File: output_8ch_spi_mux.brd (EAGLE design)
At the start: 65 x 56 mm, 50 parts, among them IC1 TPS706-1V8, IC2 5M160ZE64, IC3 SN75174SOIC-20, IC4 SN75174SOIC-20, IC6 STM32F042F, IC7 CAT24C256, Q1 50MHz

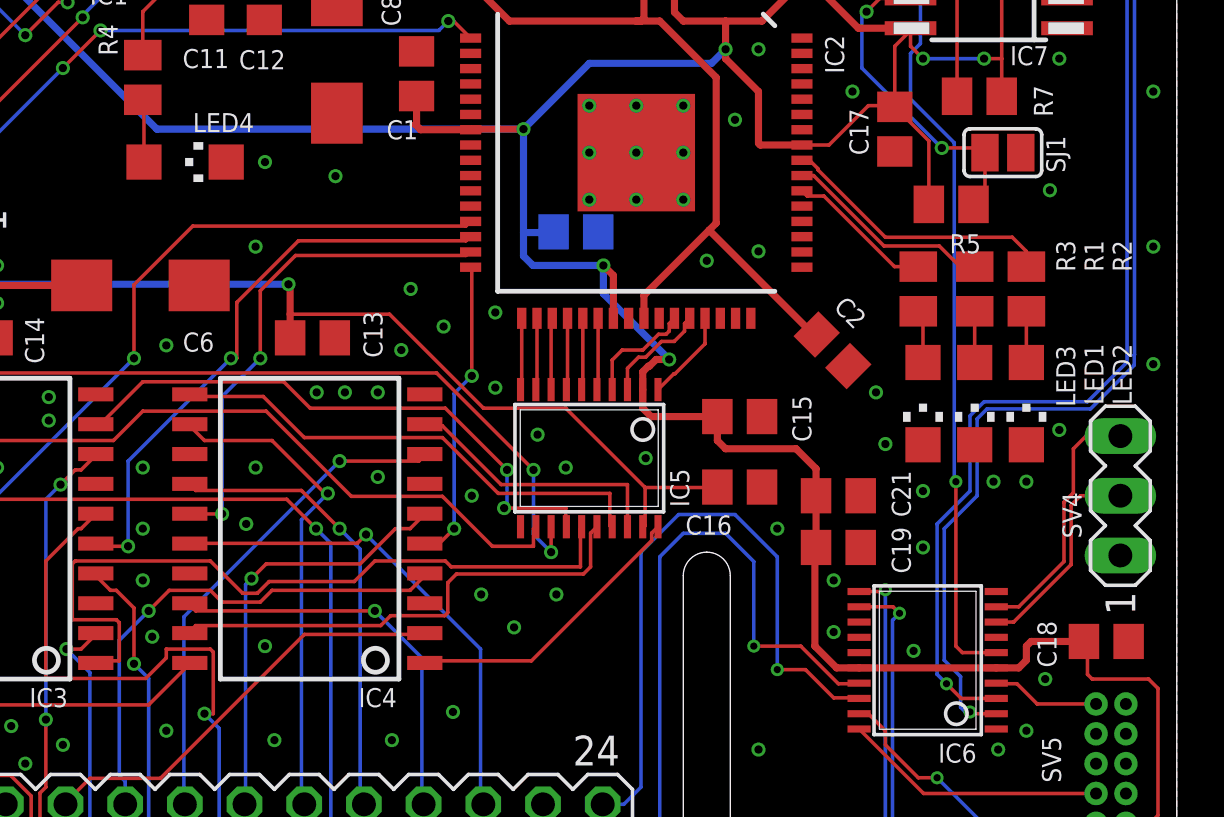
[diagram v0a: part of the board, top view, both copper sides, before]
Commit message: Added I2C testpoints
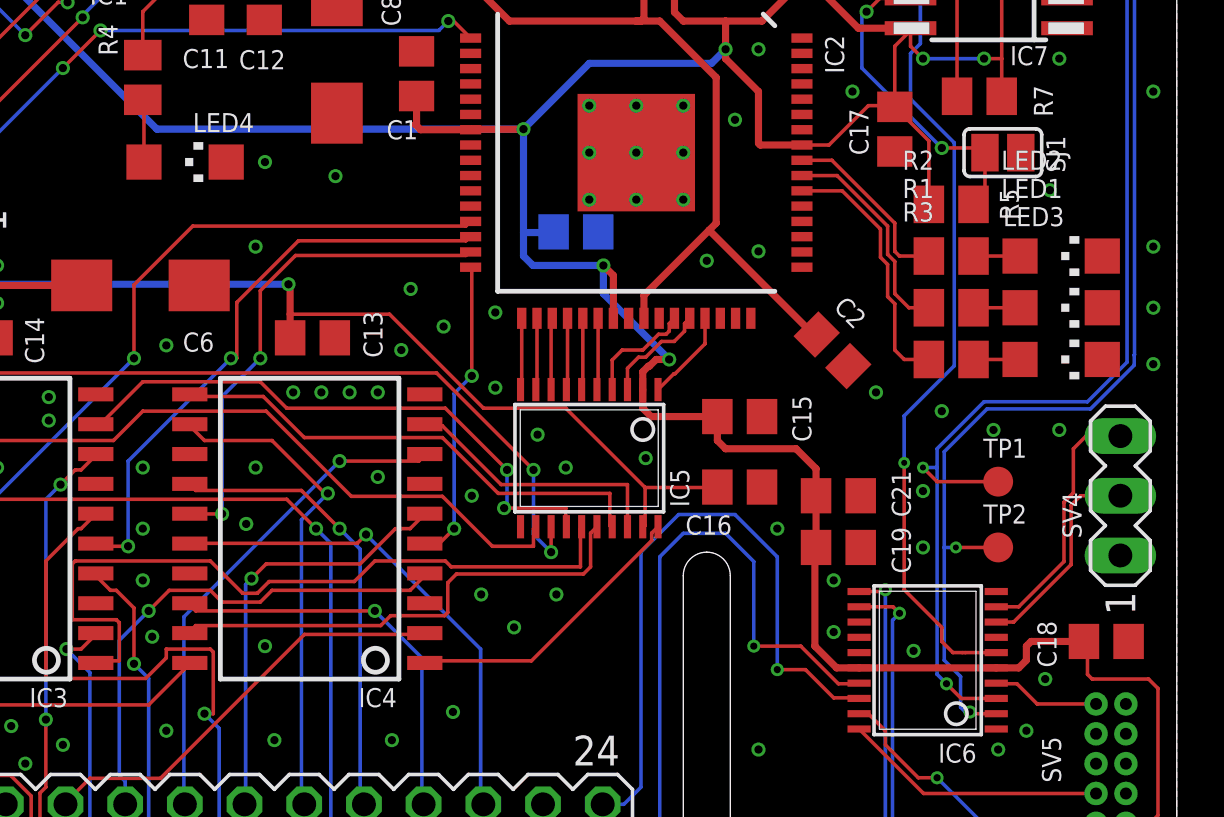
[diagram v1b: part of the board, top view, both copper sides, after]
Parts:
- added TP1, TP2: PTR1B1,27, testpad:B1,27
- moved LED2 6.45 mm to (60.1, 32.6), turned to 270 degrees
- moved LED3 6.17 mm to (60.1, 28.2), turned to 270 degrees
- moved LED1 5.49 mm to (60.1, 30.4), turned to 270 degrees
- moved R2 3.49 mm to (55.4, 32.6), turned to 0 degrees
- moved R3 3.31 mm to (55.4, 28.2), turned to 0 degrees
- moved R1 1.28 mm to (55.4, 30.4), turned to 0 degrees
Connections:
- net I2C_SCL: now also TP1.TP
- net I2C_SDA: now also TP2.TP
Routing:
- net STATUS2: track 6.29 -> 11.0 mm
- net I2C_SCL: track 99.8 -> 103.8 mm, vias 1 -> 2
- net STATUS1: track 11.8 -> 7.79 mm
- net I2C_SDA: track 103.6 -> 105.9 mm, vias 1 -> 2
- net !CAN_INT: track 38.1 -> 40.1 mm

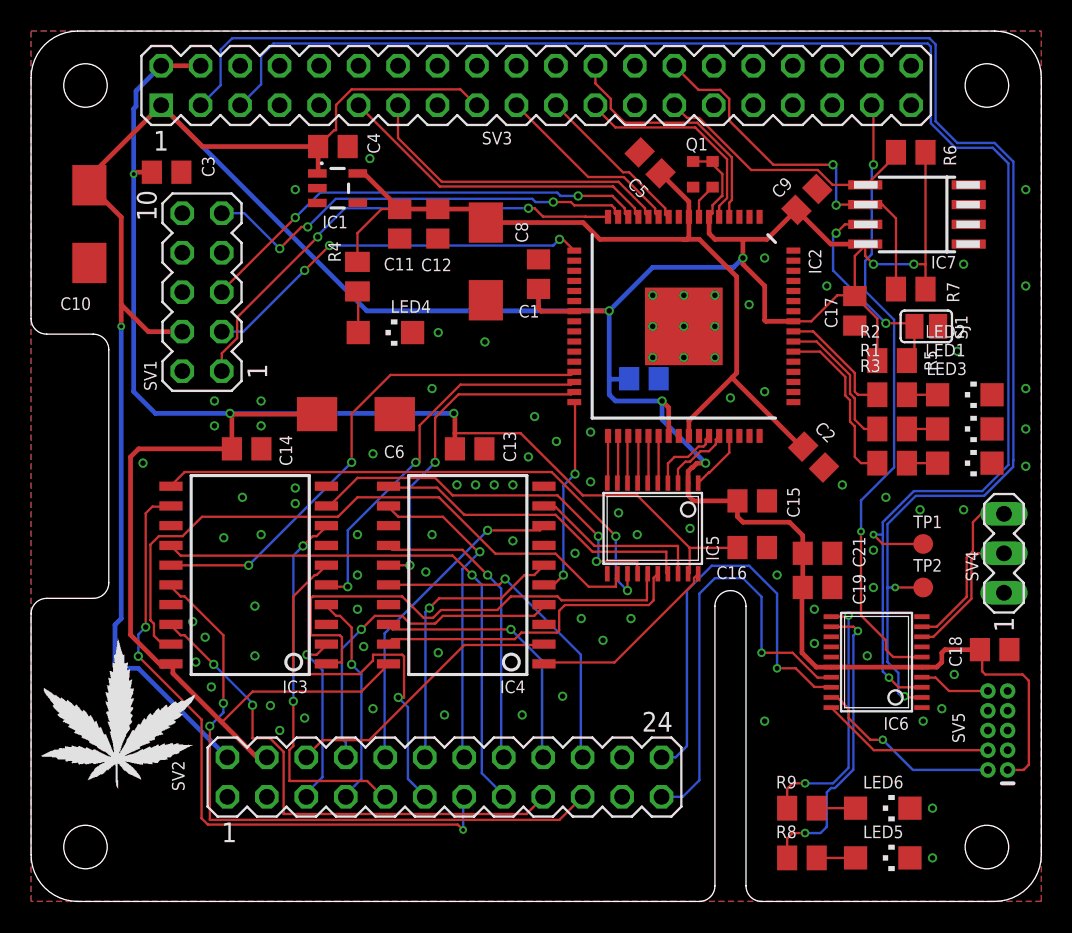
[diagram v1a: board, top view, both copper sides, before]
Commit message: Added clock calibration signal to cannabus controller (divide 50MHz clk by 1000 in CPLD)
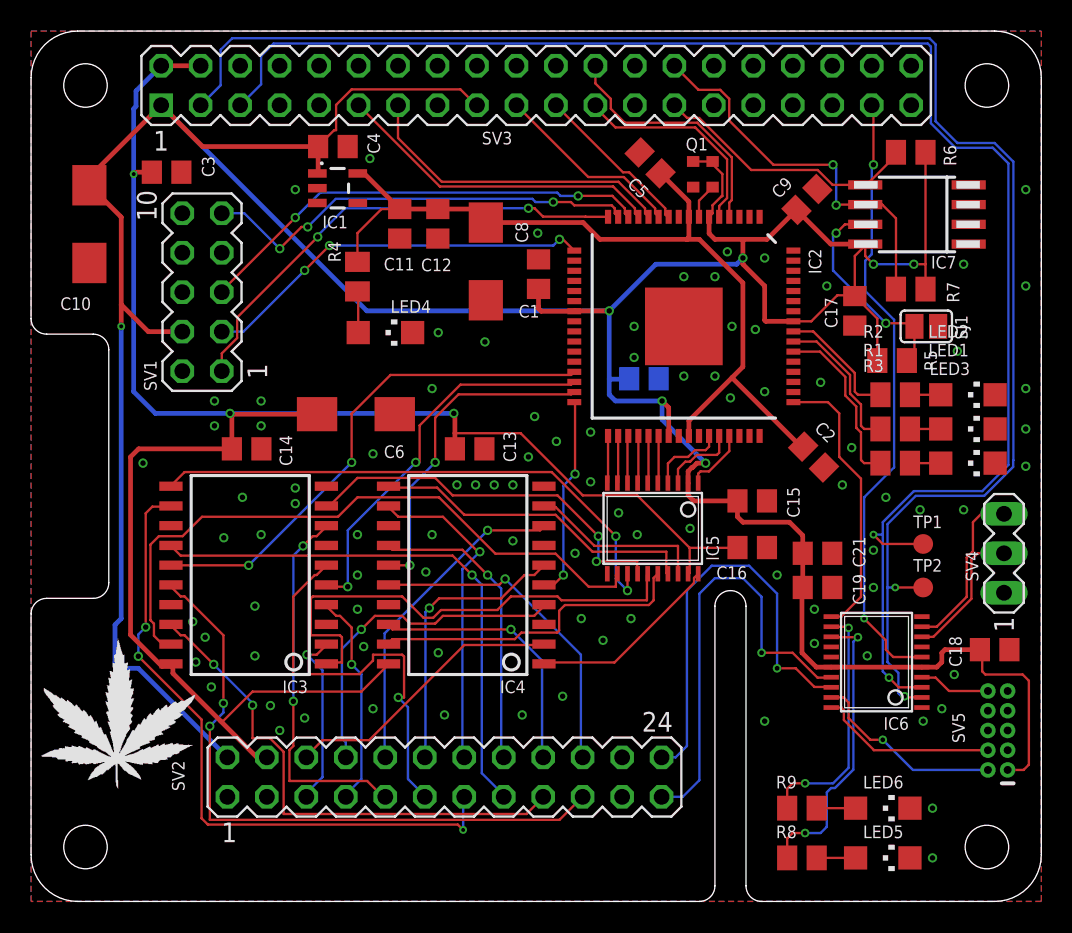
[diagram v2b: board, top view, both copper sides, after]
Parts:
- moved LED1 0.20 mm to (60.3, 30.4)
- moved LED2 0.20 mm to (60.3, 32.6)
- moved LED3 0.20 mm to (60.3, 28.2)
- moved R1 0.20 mm to (55.6, 30.4)
- moved R2 0.20 mm to (55.6, 32.6)
- moved R3 0.20 mm to (55.6, 28.2)
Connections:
- new net OSC_CAL_CLK: IC2.49, IC6.11
- net CORTEX_STATUS0: now also IC6.13; no longer IC6.12
- net CORTEX_STATUS1: now also IC6.12; no longer IC6.11
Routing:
- net OSC_CAL_CLK: track 0.00 -> 18.1 mm
- net CORTEX_STATUS1: track 16.7 -> 15.9 mm
- net CORTEX_SWDIO: track 12.4 -> 13.0 mm
- net CORTEX_STATUS0: track 19.5 -> 19.0 mm

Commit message: Cleaned up output and differential driver boards; added basic differential receiver board
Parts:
- moved C4 2.33 mm to (18.2, 46.6)
- moved IC1 2.33 mm to (18.5, 43.9)
- moved C1 1.00 mm to (31.6, 40.4)
- moved C8 0.82 mm to (28.5, 41.4)
- moved C12 0.82 mm to (25.4, 43.8)
- moved C11 0.45 mm to (23.3, 43.8)
- moved C3 0.40 mm to (8.72, 47.3)
- moved R5 0.20 mm to (55.6, 34.8)
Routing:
- net +3V3: track 243.8 -> 249.4 mm, vias 7 -> 8
- net CPLD_TDI: track 28.4 -> 30.6 mm
- net CPLD_TDO: track 25.4 -> 27.2 mm
- net VCORE: track 55.7 -> 54.6 mm
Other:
- board text added: "Rev 01"

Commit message: yes
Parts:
- LED5, LED6: value (none) -> GRN
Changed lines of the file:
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@@
 </class>
 </classes>
-<designrules name="oshpark-2layer">
+<designrules name="oshpark-2layer *">
 <description language="en">&lt;b&gt;OSH Park Design Rules&lt;/b&gt;
 &lt;p&gt;
@@
 <param name="checkValues" value="0"/>
 <param name="checkNames" value="1"/>
-<param name="checkWireStubs" value="1"/>
+<param name="checkWireStubs" value="0"/>
 <param name="checkPolygonWidth" value="0"/>
 <param name="useDiameter" value="13"/>
@@
 <attribute name="SPICEPREFIX" value="C" x="28.46" y="41.38" size="1.778" layer="27" rot="R270" display="off"/>
 </element>
-<element name="IC1" library="lichtenstein_onion" package="SOT23-5" value="TPS706-1V8" x="18.52" y="43.89" smashed="yes" rot="R270">
+<element name="IC1" library="lichtenstein_onion" package="SOT23-5" package3d_urn="urn:adsk.eagle:package:16456/2" value="TPS706-1V8" x="18.52" y="43.89" smashed="yes" rot="R270">
 <attribute name="MOUSER" value="595-TPS70618DBVT" x="18.52" y="43.89" size="1.778" layer="27" rot="R270" display="off"/>
 <attribute name="NAME" x="19.179" y="42.121" size="0.8128" layer="25" font="vector" ratio="10" rot="R180"/>
@@
 <attribute name="NAME" x="50.035" y="42" size="0.8128" layer="25" font="vector" ratio="10" rot="R270"/>
 </element>
-<element name="IC5" library="lichtenstein_onion" package="TSSOP20" value="" x="40" y="24" smashed="yes" rot="R180">
+<element name="IC5" library="lichtenstein_onion" package="TSSOP20" package3d_urn="urn:adsk.eagle:package:4349/2" value="" x="40" y="24" smashed="yes" rot="R180">
 <attribute name="MOUSER" value="595-TXB0108PWR" x="40" y="24" size="1.778" layer="27" rot="R180" display="off"/>
 <attribute name="NAME" x="44.2544" y="21.9172" size="0.8128" layer="25" font="vector" ratio="10" rot="R90"/>
@@
 <attribute name="SPICEPREFIX" value="C" x="50.6" y="20.2" size="1.778" layer="27" display="off"/>
 </element>
-<element name="IC6" library="lichtenstein_onion" package="TSSOP20" value="STM32F042F" x="54.4" y="15.4" smashed="yes" rot="R90">
+<element name="IC6" library="lichtenstein_onion" package="TSSOP20" package3d_urn="urn:adsk.eagle:package:4349/2" value="STM32F042F" x="54.4" y="15.4" smashed="yes" rot="R90">
 <attribute name="MOUSER" value="511-STM32F042F6P6" x="54.4" y="15.4" size="1.016" layer="27" rot="R90" display="off"/>
 <attribute name="NAME" x="56.4828" y="11.8544" size="0.8128" layer="25" ratio="10" rot="R180"/>
 </element>
-<element name="LED5" library="led" library_urn="urn:adsk.eagle:library:259" package="CHIPLED_1206" package3d_urn="urn:adsk.eagle:package:15823/2" value="" x="54.8" y="2.8" smashed="yes" rot="R270">
+<element name="LED5" library="led" library_urn="urn:adsk.eagle:library:259" package="CHIPLED_1206" package3d_urn="urn:adsk.eagle:package:15823/2" value="GRN" x="54.8" y="2.8" smashed="yes" rot="R270">
 <attribute name="MOUSER" value="604-APTR3216SGC" x="66.8" y="9.2" size="1.016" layer="27" rot="R270" display="off"/>
 <attribute name="NAME" x="53.53" y="4.07" size="0.8128" layer="25" ratio="10"/>
-<attribute name="VALUE" x="53.53" y="0.26" size="1.27" layer="27"/>
 </element>
 <element name="R8" library="rcl" library_urn="urn:adsk.eagle:library:334" package="M0805" package3d_urn="urn:adsk.eagle:package:23556/1" value="680R" x="49.6" y="2.8" smashed="yes">
@@
 <attribute name="SPICEPREFIX" value="R" x="49.6" y="6" size="1.016" layer="27" display="off"/>
 </element>
-<element name="LED6" library="led" library_urn="urn:adsk.eagle:library:259" package="CHIPLED_1206" package3d_urn="urn:adsk.eagle:package:15823/2" value="" x="54.8" y="6" smashed="yes" rot="R270">
+<element name="LED6" library="led" library_urn="urn:adsk.eagle:library:259" package="CHIPLED_1206" package3d_urn="urn:adsk.eagle:package:15823/2" value="GRN" x="54.8" y="6" smashed="yes" rot="R270">
 <attribute name="MOUSER" value="604-APTR3216SGC" x="54.8" y="6" size="1.016" layer="27" rot="R270" display="off"/>
 <attribute name="NAME" x="53.53" y="7.27" size="0.8128" layer="25" ratio="10"/>
-<attribute name="VALUE" x="53.53" y="3.46" size="1.27" layer="27"/>
 </element>
 <element name="SV4" library="con-lstb" library_urn="urn:adsk.eagle:library:162" package="MA03-1" package3d_urn="urn:adsk.eagle:package:8339/1" value="" x="62.6" y="22.4" smashed="yes" rot="R90">
@@
 <wire x1="40.50175" y1="46.848246875" x2="42.325" y2="45.024996875" width="0.3048" layer="1"/>
 <wire x1="42.325" y1="45.024996875" x2="42.325" y2="44.05" width="0.3048" layer="1"/>
-<wire x1="19.8201" y1="44.84" x2="21" y2="44.84" width="0.3048" layer="1"/>
+<wire x1="19.826" y1="44.84" x2="21" y2="44.84" width="0.3048" layer="1"/>
 <wire x1="21" y1="44.84" x2="23.31" y2="44.84" width="0.3048" layer="1"/>
 <wire x1="23.31" y1="44.84" x2="23.4" y2="44.75" width="0.3048" layer="1"/>
@@
 <via x="15.4" y="44.8" extent="1-16" drill="0.35"/>
 <wire x1="15.4" y1="44.8" x2="17.1799" y2="44.8" width="0.3048" layer="1"/>
-<wire x1="17.1799" y1="44.8" x2="17.2199" y2="44.84" width="0.3048" layer="1"/>
+<wire x1="17.1799" y1="44.8" x2="17.214" y2="44.84" width="0.3048" layer="1"/>
 <wire x1="17.27" y1="46.57" x2="17.2199" y2="46.5199" width="0.3048" layer="1"/>
-<wire x1="17.2199" y1="46.5199" x2="17.2199" y2="44.84" width="0.3048" layer="1"/>
+<wire x1="17.2199" y1="46.5199" x2="17.214" y2="44.84" width="0.3048" layer="1"/>
 <wire x1="28.69" y1="49.89" x2="28.4" y2="49.6" width="0.3048" layer="16"/>
 <wire x1="28.69" y1="49.89" x2="28.69" y2="51.23" width="0.3048" layer="16"/>
@@
 <wire x1="52" y1="28.6" x2="53.4" y2="27.2" width="0.1524" layer="1"/>
 <wire x1="53.4" y1="27.2" x2="53.4" y2="19.6" width="0.1524" layer="1"/>
-<wire x1="52.125" y1="18.325" x2="51.4822" y2="18.325" width="0.1524" layer="1"/>
 <wire x1="51.275" y1="32.125" x2="52" y2="31.4" width="0.1524" layer="1"/>
 <wire x1="52" y1="31.4" x2="52" y2="28.6" width="0.1524" layer="1"/>
 <wire x1="53.4" y1="19.6" x2="52.125" y2="18.325" width="0.1524" layer="1"/>
+<wire x1="52.125" y1="18.325" x2="51.4822" y2="18.325" width="0.1524" layer="1"/>
 </signal>
 </signals>

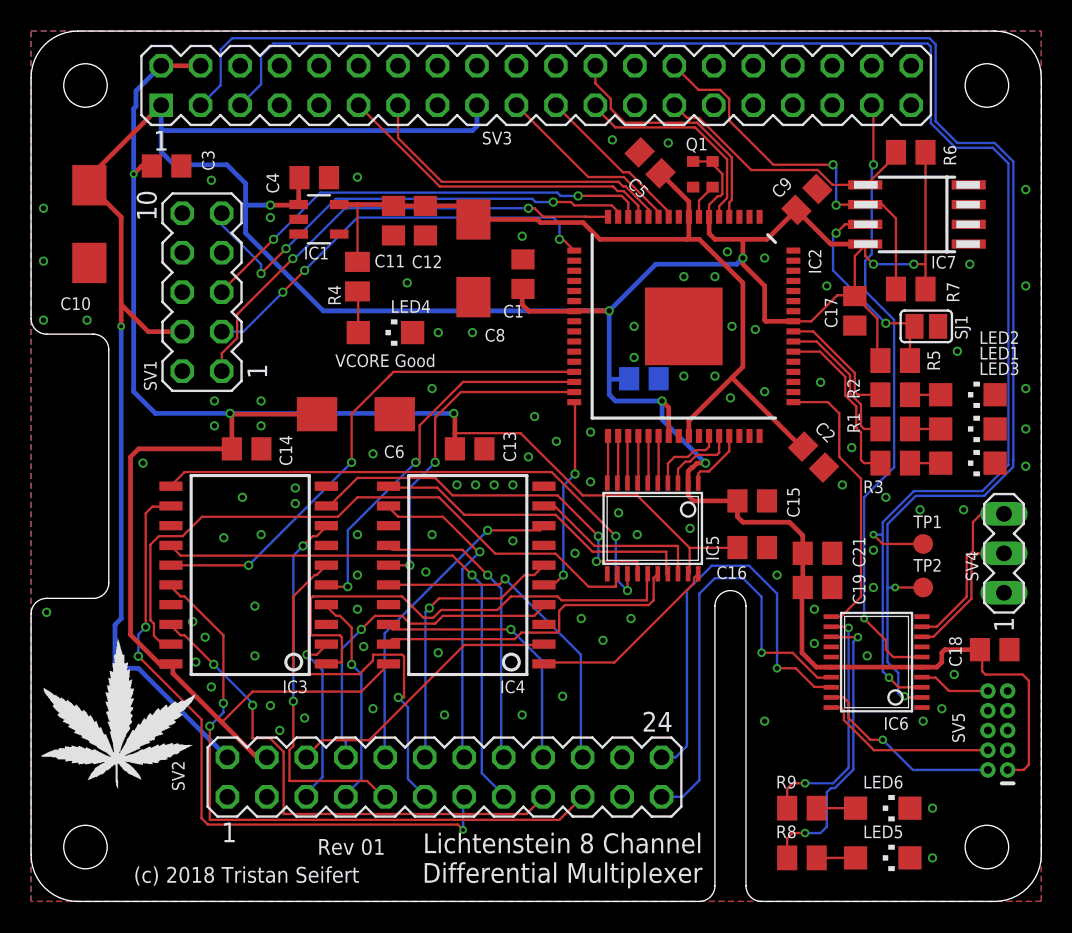
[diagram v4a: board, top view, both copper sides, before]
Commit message: rev01 of output_8ch_spi_mux sent to manufacturing
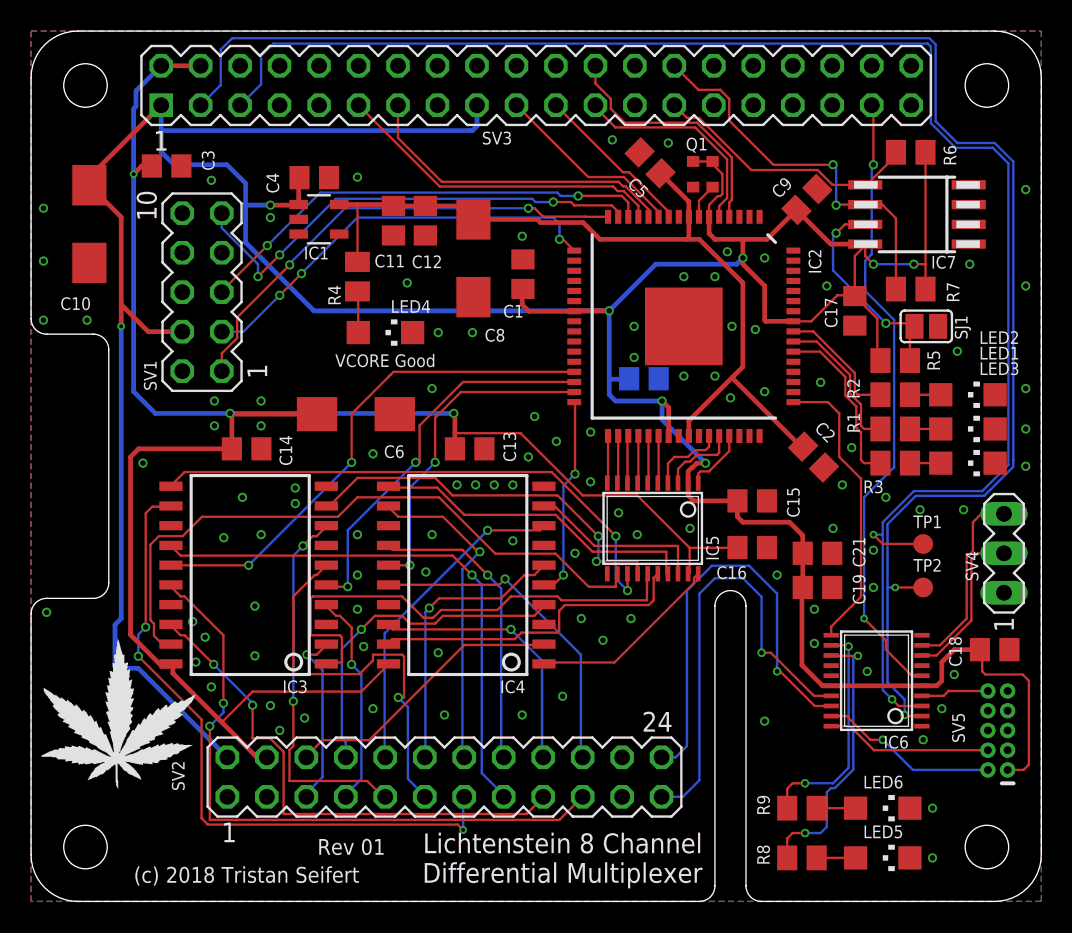
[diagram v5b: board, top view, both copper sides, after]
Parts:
- moved IC6 1.20 mm to (54.4, 14.2)
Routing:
- net +3V3: track 249.3 -> 251.5 mm
- net CORTEX_UART_TX: track 8.99 -> 10.3 mm
- net CORTEX_UART_RX: track 10.9 -> 12.2 mm
- net I2C_SCL: track 103.8 -> 105.0 mm
- net CORTEX_STATUS1: track 15.9 -> 14.7 mm
- net I2C_SDA: track 105.9 -> 107.0 mm
- net CORTEX_STATUS0: track 19.0 -> 17.9 mm
- net CORTEX_SWDIO: track 12.6 -> 11.6 mm
- net CORTEX_SWCLK: track 11.6 -> 10.7 mm
- net OSC_CAL_CLK: track 18.1 -> 18.9 mm
- net CAN_TX: track 27.9 -> 28.5 mm
